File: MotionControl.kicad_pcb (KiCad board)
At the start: 2 copper layers, 180 x 80 mm, 195 parts, among them J1 Screw_Terminal_01x02, J10 Screw_Terminal_01x02, J11 Screw_Terminal_01x02, J12 Conn_01x07_MountingPin, J13 Conn_01x07_MountingPin, J14 Conn_01x07_MountingPin, J15 Conn_01x05_Pin, J16 Conn_01x03_MountingPin, J17 Conn_01x03_MountingPin, J18 Conn_01x03_MountingPin, J19 Conn_01x03_MountingPin, J2 Conn_ARM_JTAG_SWD_10, J20 Conn_01x03_MountingPin, J21 Conn_01x03_MountingPin, J22 Conn_01x03_MountingPin, J23 Conn_01x03_MountingPin, J24 Conn_01x03_MountingPin, J25 Conn_01x03_MountingPin, J26 Conn_01x03_MountingPin, J27 Conn_01x03_MountingPin, J28 Conn_01x04_MountingPin, J29 Conn_01x03_MountingPin, J3 Screw_Terminal_01x04, J4 Conn_01x07_MountingPin, J5 Screw_Terminal_01x04, J6 Screw_Terminal_01x04, J7 Screw_Terminal_01x04, J8 Screw_Terminal_01x02, J9 Screw_Terminal_01x02, P1 USB_C_Plug_USB2.0, Q1 2N7002, Q10 Q_NMOS_DGS, Q11 Q_NMOS_DGS, Q12 Q_NMOS_DGS, Q13 Q_NMOS_DGS, Q14 Q_NMOS_DGS, Q15 Q_NMOS_DGS, Q16 Q_NMOS_DGS, Q17 Q_NMOS_DGS, Q18 Q_NMOS_DGS, Q19 Q_NMOS_DGS, Q2 Q_NMOS_DGS, Q20 Q_NMOS_DGS, Q21 Q_NMOS_DGS, Q22 Q_NMOS_DGS, Q23 Q_NMOS_DGS, Q24 Q_NMOS_DGS, Q25 Q_NMOS_DGS, Q26 Q_NMOS_DGS, Q27 Q_NMOS_DGS, Q28 Q_NMOS_DGS, Q29 Q_NMOS_DGS, Q3 Q_NMOS_DGS, Q30 Q_NMOS_DGS, Q31 Q_NMOS_DGS, Q32 Q_NMOS_DGS, Q33 Q_NMOS_DGS, Q4 Q_NMOS_DGS, Q5 Q_NMOS_DGS, Q6 Q_NMOS_DGS, Q7 Q_NMOS_DGS, Q8 Q_NMOS_DGS, Q9 Q_NMOS_DGS, SW1 SW_Push, U1 ATSAMD21J18A-A, U2 AP2112K-3.3, U3 TMC5160A-TA, U4 TMC5160A-TA, U5 TMC5160A-TA, U6 TMC5160A-TA, U7 TC4427, Y1 32.768kHz

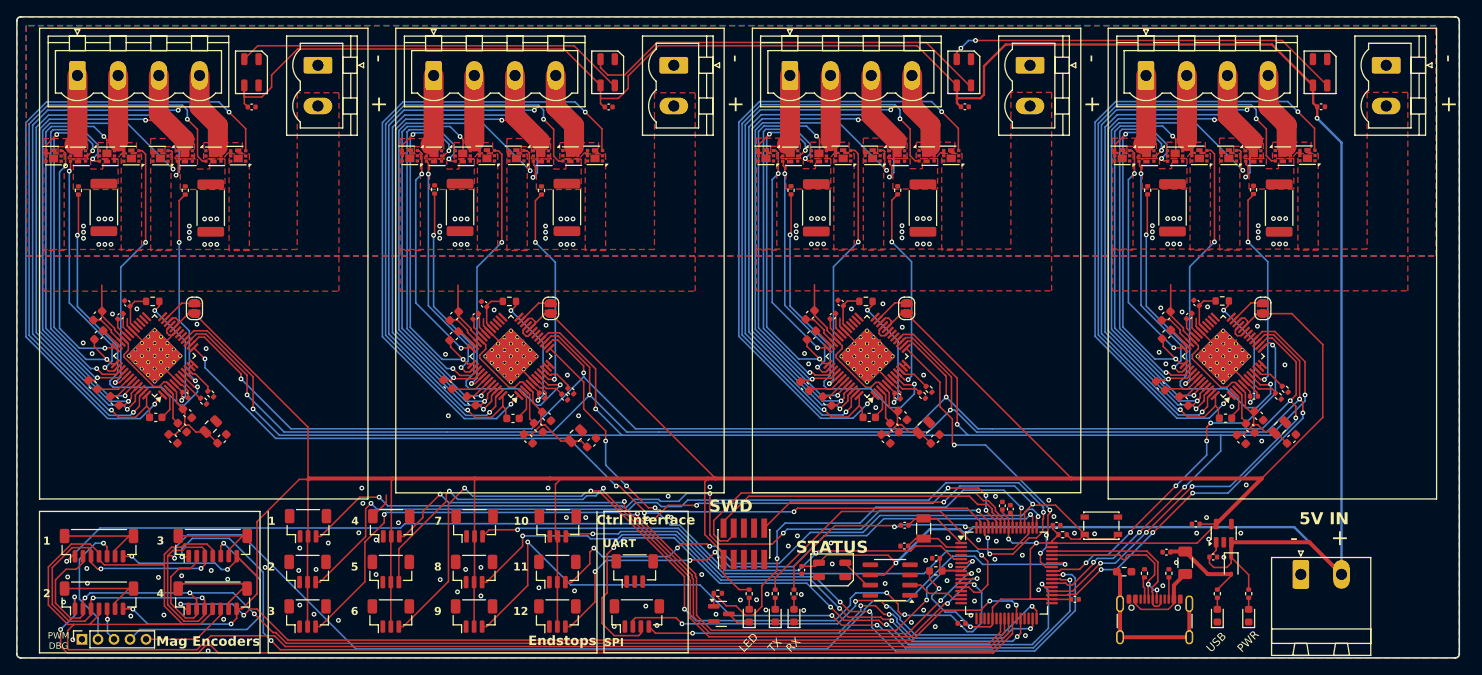
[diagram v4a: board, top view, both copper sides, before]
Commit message: add spi cs pin, remove center endstop support
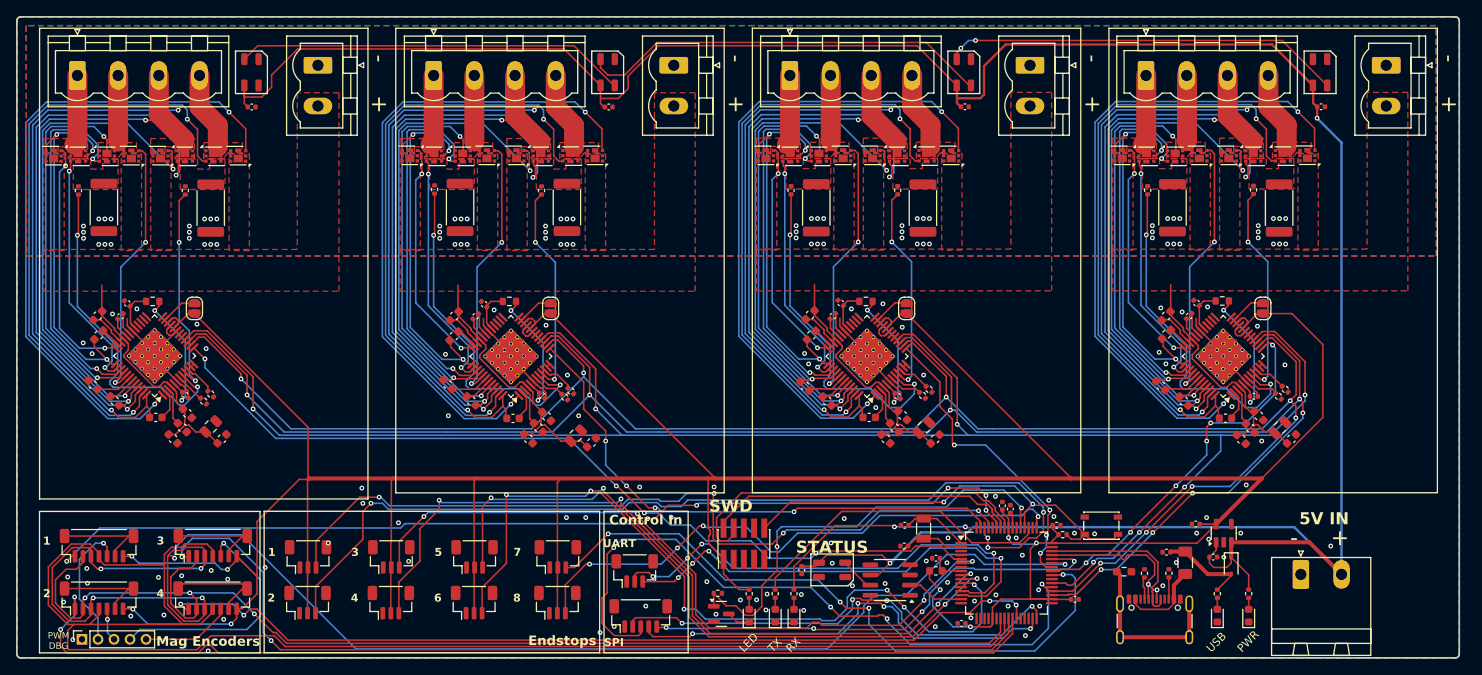
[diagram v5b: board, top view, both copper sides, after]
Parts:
- removed J18, J21, J24, J27: Conn_01x03_MountingPin, Connector_JST:JST_SH_BM03B-SRSS-TB_1x03-1MP_P1.00mm_Vertical
- J28: footprint Connector_JST:JST_SH_BM04B-SRSS-TB_1x04-1MP_P1.00mm_Vertical -> Connector_JST:JST_SH_BM05B-SRSS-TB_1x05-1MP_P1.00mm_Vertical
- moved J17 3.88 mm to (69.3, 93.4)
- moved J20 3.88 mm to (79.7, 93.4)
- moved J23 3.88 mm to (90.1, 93.4)
- moved J26 3.88 mm to (100.5, 93.4)
- moved J16 3.88 mm to (69.4, 87.7)
- moved J19 3.88 mm to (79.7, 87.7)
- moved J22 3.88 mm to (90.1, 87.7)
- moved J25 3.88 mm to (100.5, 87.7)
- moved J28 0.48 mm to (110.9, 95.1)
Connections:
- net PB17_ES10 renamed PB17_ES8
- net PB22_ES11 renamed PB22_ES8
- J19 pad 3: PB06_ES4 -> PB05_ES3
- J20 pad 3: PB07_ES5 -> PB06_ES4
- J22 pad 3: PB06_ES7 -> PB07_ES5
- J23 pad 3: PB15_ES8 -> PB08_ES6
- J29 pad 2: unconnected-(J29-Pin_2-Pad2) -> PA04_MASTER_TX
- J29 pad 3: unconnected-(J29-Pin_3-Pad3) -> PA05_MASTER_RX
- U1 pad 12: PB06_ES7 -> unconnected-(U1-PB09-Pad12)
- U1 pad 13: unconnected-(U1-PA04-Pad13) -> PA04_MASTER_TX
- U1 pad 14: unconnected-(U1-PA05-Pad14) -> PA05_MASTER_RX
- U1 pad 28: PB15_ES8 -> unconnected-(U1-PB15-Pad28)
- U1 pad 39: PB16_ES9 -> unconnected-(U1-PB16-Pad39)
- U1 pad 44: unconnected-(U1-PA23-Pad44) -> PA23_MASTER_CS
- U1 pad 50: PB23_ES12 -> unconnected-(U1-PB23-Pad50)
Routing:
- net PB16_ES9: track 94.4 -> 0.00 mm, vias 4 -> 0
- net PB15_ES8: track 78.5 -> 0.00 mm, vias 4 -> 0
- net PB06_ES7: track 74.4 -> 0.00 mm, vias 2 -> 0
- net PB23_ES12: track 69.3 -> 0.00 mm, vias 4 -> 0
- net PA23_MASTER_CS: track 0.00 -> 59.7 mm, vias 0 -> 4
- net PA04_MASTER_TX: track 0.00 -> 59.0 mm, vias 0 -> 4
- net PA05_MASTER_RX: track 0.00 -> 57.7 mm, vias 0 -> 4
- net PB05_ES3: track 106.6 -> 91.1 mm
- net PB07_ES5: track 96.7 -> 86.3 mm
- net PB08_ES6: track 107.0 -> 96.7 mm
- net +3V3: track 488.4 -> 479.7 mm
- net PB06_ES4: track 89.2 -> 97.5 mm
- net PB00_ES1: track 96.2 -> 100.0 mm
- net GND: track 104.1 -> 100.8 mm, vias 186 -> 169
- net PB22_ES8: track 68.5 -> 71.1 mm
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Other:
- board text added: "Control In"
- board text removed: "10"
- board text removed: "11"
- board text removed: "12"
- board text removed: "9"
- board text removed: "Ctrl Interface"
